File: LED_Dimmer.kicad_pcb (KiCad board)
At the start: 2 copper layers, 34.5 x 35.8 mm, 23 parts, among them J1 2.54mm Header, J2 2.54mm Header, Q1 PJA3404A_R1_00001, U1 TLC555CDR

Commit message: Fix diode part number
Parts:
- D1, D2: value 1N4148 -> 1N4148W
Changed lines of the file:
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@@
 			)
 		)
-		(property "Value" "1N4148"
+		(property "Value" "1N4148W"
 			(at 0 2.1 0)
 			(layer "F.Fab")
@@
 			)
 		)
-		(property "Value" "1N4148"
+		(property "Value" "1N4148W"
 			(at 0 2.1 0)
 			(layer "F.Fab")

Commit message: Add current limiting resistor to FET
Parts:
- added R2: 1K, Resistor_SMD:R_0805_2012Metric_Pad1.20x1.40mm_HandSolder, F.Cu at (101.5, 38.9)
- moved D3 4.81 mm to (101.7, 43.6), turned to -90 degrees
- moved Q1 2.36 mm to (104.5, 40.2)
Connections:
- Q1 pad 2: /PWM -> Net-(Q1-G)
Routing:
- net 12V: track 42.8 -> 35.3 mm
- net 12V_RPP: track 14.3 -> 18.7 mm
- net /SwitchGND: track 19.1 -> 23.4 mm
- net Net-(Q1-G): track 0.00 -> 2.73 mm
- net /PWM: track 7.22 -> 4.66 mm
- net GND: vias 66 -> 64
- removed copper zone on F.Cu, net /SwitchGND

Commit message: Add optional regulator for 24V LEDs
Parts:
- added C3: 100nF, Capacitor_SMD:C_0805_2012Metric_Pad1.18x1.45mm_HandSolder, F.Cu at (112.4, 32.2)
- added JP1: SolderJumper_2_Open, Jumper:SolderJumper-2_P1.3mm_Open_RoundedPad1.0x1.5mm, F.Cu at (115.3, 31.5)
- added U2: ZXTR2012Z, Package_TO_SOT_SMD:SOT-89-3, F.Cu at (116.2, 35.9)
- moved D3 14.9 mm to (116.1, 40.2), turned to 180 degrees
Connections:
- net 12V renamed Vin
- D3 pad 1: 12V_RPP -> Net-(D3-K)
- R1 pad 1: 12V_RPP -> Vcc
- U1 pad 4: 12V_RPP -> Vcc
- U1 pad 8: 12V_RPP -> Vcc
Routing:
- net Vcc: track 0.00 -> 19.2 mm
- net 12V_RPP: track 18.7 -> 0.00 mm
- net Net-(D3-K): track 0.00 -> 9.43 mm
- net Vin: track 35.3 -> 41.1 mm, vias 0 -> 1
- net /DISCH: track 11.4 -> 9.65 mm
- net GND: vias 64 -> 55
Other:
- board text added: "5-24V 5A"
- board text removed: "5-12V,5A"

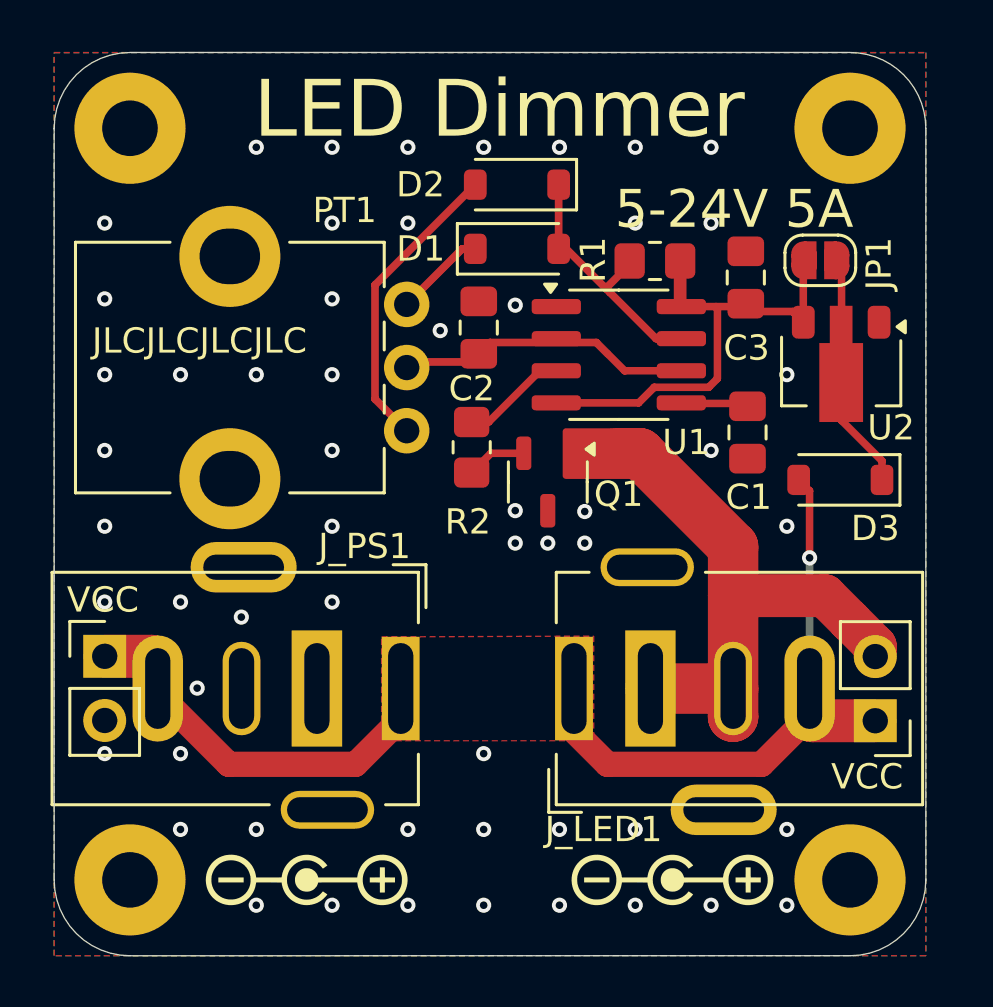
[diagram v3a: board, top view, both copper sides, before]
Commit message: Fix MOSFET pin order
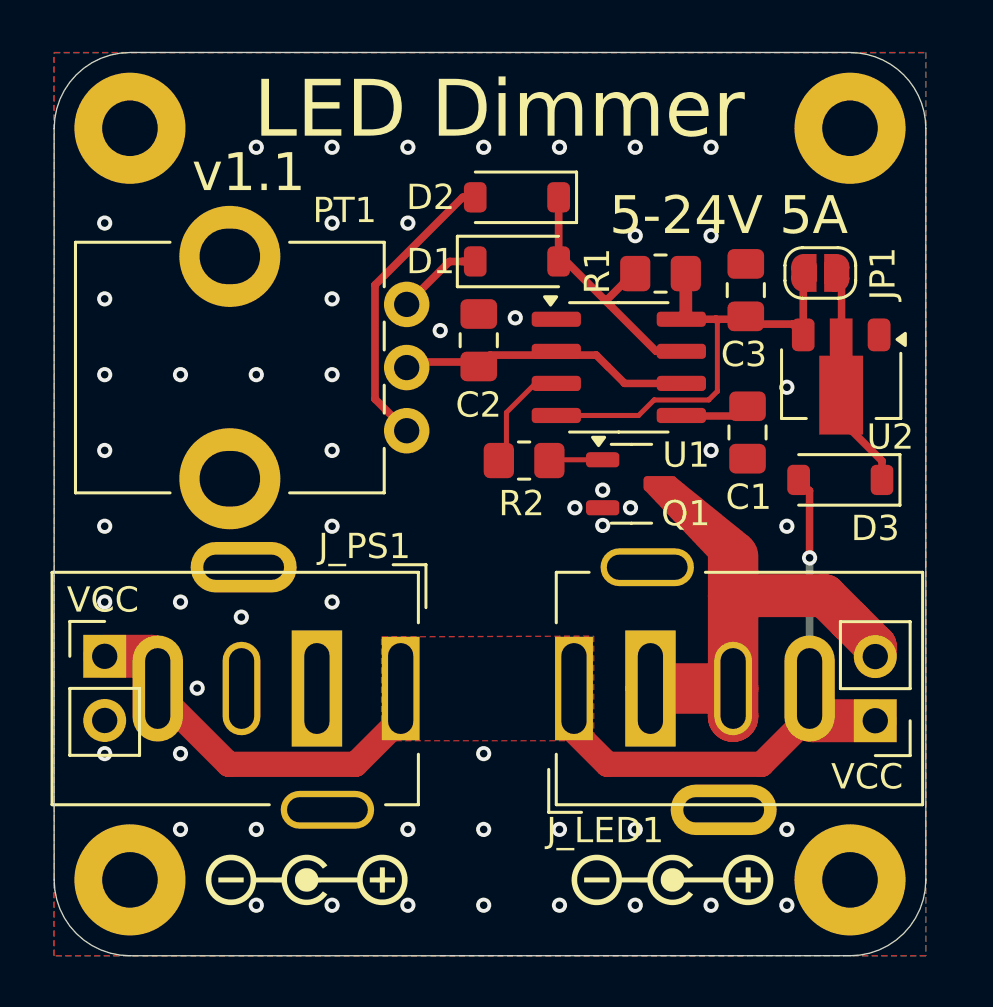
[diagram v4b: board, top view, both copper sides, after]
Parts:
- moved Q1 3.31 mm to (107.8, 40.3), turned to 0 degrees
- moved R2 2.14 mm to (103.6, 39.4), turned to 0 degrees
- moved R1 0.55 mm to (109.0, 32.0)
- moved C2 0.50 mm to (101.8, 34.6)
- moved C3 0.50 mm to (112.4, 32.7)
- moved D1 0.50 mm to (103.3, 31.5)
- moved D2 0.50 mm to (103.3, 29.0)
- moved JP1 0.50 mm to (115.3, 32.0)
- moved U1 0.50 mm to (107.3, 35.7)
- moved U2 0.50 mm to (116.2, 36.4)
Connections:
- Q1 pad 1: /SwitchGND -> Net-(Q1-G)
- Q1 pad 2: Net-(Q1-G) -> GND
- Q1 pad 3: GND -> /SwitchGND
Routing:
- net /SwitchGND: track 23.4 -> 16.9 mm
- net Net-(D3-K): track 9.43 -> 5.64 mm
- net Net-(Q1-G): track 2.73 -> 2.12 mm
- net GND: vias 55 -> 54
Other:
- board text added: "v1.1"
- board text removed: "JLCJLCJLCJLC"
